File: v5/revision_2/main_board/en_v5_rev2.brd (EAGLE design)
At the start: 57.8 x 34 mm, 183 parts, among them J1 M50-3142045THT, J2 M50-3142045THT, J3 53261-0271, J4 USB4105-GF-A, J5 FEMALE_HEADER_2X1, M1 SISS23DN, M2 SISS23DN, Q1 FDN302P, U1 REF3012AIDBZR, U10 CY7C1051DV33, U2 MCP73833T-AMI/MF, U3 LTC3569EUDPBF, U4 PAC1934, U5 PAC1934, U6 W25Q16JVUXIQ, U7 RP2040, U8 SPARTAN7-LX15, U9 S25FL256S, X1 12MHz, X2 32MHz, X3 100MHz

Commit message: change vias position
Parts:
- moved R32 0.70 mm to (17.8, 26.2)
- moved R35 0.70 mm to (17.8, 25.0)
- moved C24 0.65 mm to (15.3, 16.8)
- moved R48 0.60 mm to (38.8, 16.1)
- moved C34 0.50 mm to (53.1, 4.74)
- moved C35 0.50 mm to (51.1, 4.74)
- moved R45 0.30 mm to (17.7, 13.0)
- moved C23 0.11 mm to (23.0, 22.1)
- turned C14 to 0 degrees
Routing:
- net VCC_3V3: track 138.9 -> 149.0 mm, vias 12 -> 13
- net PIO6/I2C1_SDA: track 64.9 -> 63.3 mm
- net PIO2/SPI2FLASH_SCK(SPI0): track 60.7 -> 62.2 mm
- net !USB_BOOT: track 17.9 -> 19.4 mm
- net FPGA_VCC_1V: track 90.8 -> 89.4 mm, vias 19 -> 16
- net FPGA_VCC_1V8: track 74.4 -> 75.7 mm, vias 12 -> 11
- net SPI2FLASH_DQ3: track 8.86 -> 10.1 mm
- net VCC_MCU: track 106.1 -> 107.3 mm, vias 15 -> 17
- net !MCU_RST: track 32.5 -> 33.5 mm
- net MCU_QSPI_SS: track 4.55 -> 5.55 mm
- net VCC_30_34: track 51.0 -> 50.3 mm
- net VCC_30_14: track 126.1 -> 126.7 mm
- net PIO7/I2C1_SCL: track 68.1 -> 67.4 mm
- net MCU_1V1: track 19.0 -> 19.7 mm
- net N$16: track 0.57 -> 1.14 mm
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
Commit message: optimize design half done
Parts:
- moved M1 1.00 mm to (41.0, 30.1)
- moved M2 1.00 mm to (47.0, 30.1)
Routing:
- net FPGA_VCCIO_MON: track 24.0 -> 21.2 mm
- net FPGA_VCC_1V8: track 75.7 -> 74.0 mm
- net VCC_30_34: track 50.3 -> 49.0 mm
- net PIO21/!PWR_FPGA_IO_SRAM: track 30.2 -> 29.1 mm
- net FPGA_VCC_SRAM_MON: track 29.5 -> 30.1 mm

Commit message: changed a resistor value
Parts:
- R4: value 10K -> 0R
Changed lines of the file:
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@@
 <drawing>
 <settings>
-<setting alwaysvectorfont="yes"/>
+<setting alwaysvectorfont="no"/>
 <setting verticaltext="up"/>
 </settings>
@@
 <attribute name="OC_NEWARK" value="unknown" x="12.4" y="27.3888875" size="1.778" layer="27" display="off"/>
 </element>
-<element name="R4" library="passive" package="0402" package3d_urn="urn:adsk.eagle:package:27538107/2" value="10K" x="12.4" y="26.1" smashed="yes">
+<element name="R4" library="passive" package="0402" package3d_urn="urn:adsk.eagle:package:27538107/2" value="0R" x="12.4" y="26.1" smashed="yes">
 <attribute name="MF" value="" x="12.4" y="26.1" size="1.778" layer="27" display="off"/>
 <attribute name="MPN" value="" x="12.4" y="26.1" size="1.778" layer="27" display="off"/>

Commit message: fixed the voltage regulator
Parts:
- C1, C5, C6: value 10uF -> 0.1uF
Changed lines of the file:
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@@
 <attribute name="OC_NEWARK" value="unknown" x="24.2" y="19.6" size="1.778" layer="28" rot="MR90" display="off"/>
 </element>
-<element name="C1" library="passive" package="0805" package3d_urn="urn:adsk.eagle:package:27555303/2" value="10uF" x="12.9615" y="24.5" smashed="yes" rot="R180">
+<element name="C1" library="passive" package="0805" package3d_urn="urn:adsk.eagle:package:27555303/2" value="0.1uF" x="12.9615" y="24.5" smashed="yes" rot="R180">
 <attribute name="MF" value="" x="11.4615" y="24.5" size="1.778" layer="27" rot="R180" display="off"/>
 <attribute name="MPN" value="" x="11.4615" y="24.5" size="1.778" layer="27" rot="R180" display="off"/>
@@
 <attribute name="VALUE" x="10.85513125" y="19.51893125" size="2.083240625" layer="28" ratio="10" rot="SMR0"/>
 </element>
-<element name="C5" library="passive" package="CAPC1608-0603" package3d_urn="urn:adsk.eagle:package:27555773/1" value="10uF" x="3.7" y="28.1" smashed="yes" rot="MR270">
+<element name="C5" library="passive" package="CAPC1608-0603" package3d_urn="urn:adsk.eagle:package:27555773/1" value="0.1uF" x="3.7" y="28.1" smashed="yes" rot="MR270">
 <attribute name="MF" value="" x="3.7" y="27.7" size="1.778" layer="28" rot="MR270" display="off"/>
 <attribute name="MPN" value="" x="3.7" y="27.7" size="1.778" layer="28" rot="MR270" display="off"/>
 <attribute name="OC_NEWARK" value="unknown" x="3.7" y="27.7" size="1.778" layer="28" rot="MR270" display="off"/>
 </element>
-<element name="C6" library="passive" package="CAPC1608-0603" package3d_urn="urn:adsk.eagle:package:27555773/1" value="10uF" x="12.23" y="24.11" smashed="yes" rot="MR180">
+<element name="C6" library="passive" package="CAPC1608-0603" package3d_urn="urn:adsk.eagle:package:27555773/1" value="0.1uF" x="12.23" y="24.11" smashed="yes" rot="MR180">
 <attribute name="MF" value="" x="12.63" y="24.11" size="1.778" layer="28" rot="MR180" display="off"/>
 <attribute name="MPN" value="" x="12.63" y="24.11" size="1.778" layer="28" rot="MR180" display="off"/>

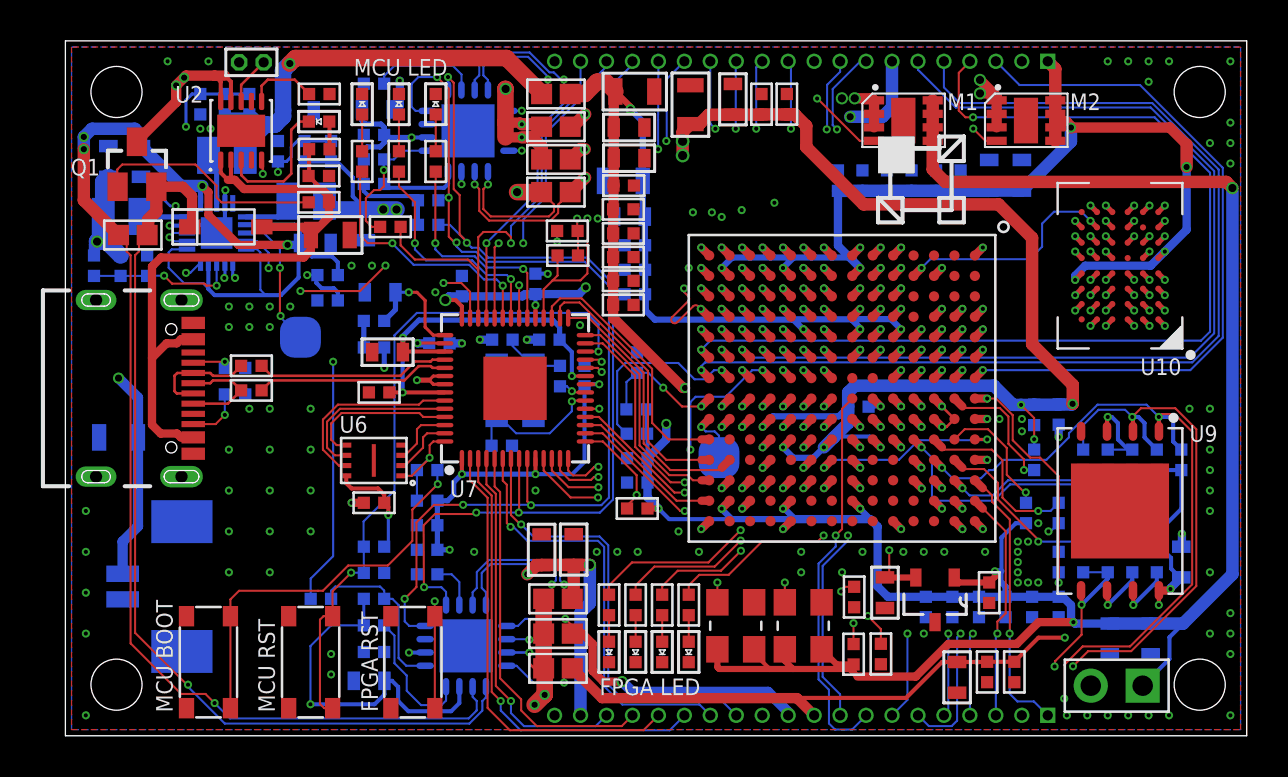
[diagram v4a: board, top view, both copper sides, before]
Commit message: changed the direction of battery connector
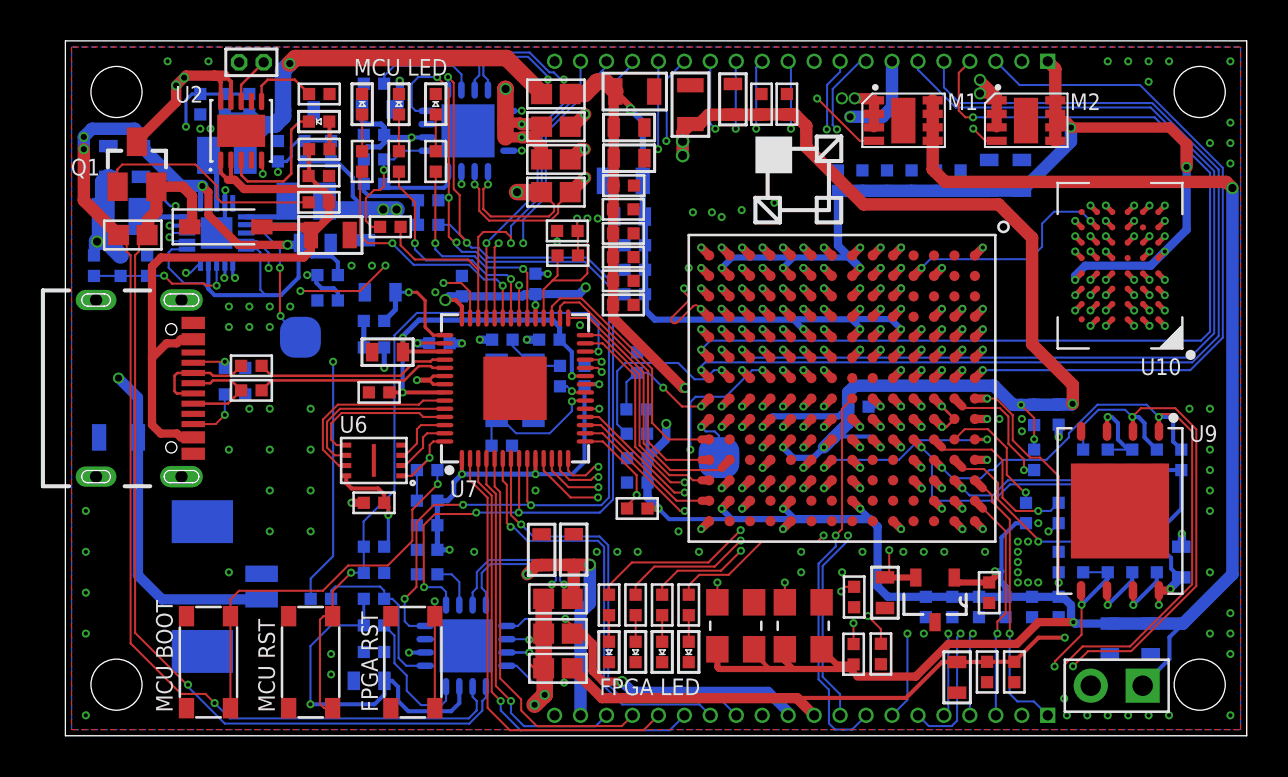
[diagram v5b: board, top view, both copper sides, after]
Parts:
- moved J3 1.00 mm to (6.70, 7.30), turned to 90 degrees
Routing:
- net VBAT: track 35.7 -> 42.0 mm
- net GND: vias 159 -> 156
